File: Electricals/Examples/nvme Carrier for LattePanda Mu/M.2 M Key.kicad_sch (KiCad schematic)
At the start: 85 parts, among them J100 Bus_M.2_Socket_M, J110 Bus_M.2_Socket_M, J120 Bus_M.2_Socket_M, J130 Bus_M.2_Socket_M, J140 Bus_M.2_Socket_M, J150 Bus_M.2_Socket_M

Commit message: Some small changes
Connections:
- net +3V3aa: now also R132.2; no longer R112.2
- net +3V3b: now also R112.2; no longer R122.2
- net +3V3bb: now also R142.2; no longer R132.2
- net +3V3c: now also R122.2; no longer R142.2
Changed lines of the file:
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@@
 			)
 		)
-		(property "Value" "+3V3c"
+		(property "Value" "+3V3bb"
 			(at 335.28 279.4 0)
 			(effects
@@
 			)
 		)
-		(property "Value" "+3V3bb"
+		(property "Value" "+3V3aa"
 			(at 163.83 275.59 0)
 			(effects
@@
 			)
 		)
-		(property "Value" "+3V3b"
+		(property "Value" "+3V3c"
 			(at 527.05 107.95 0)
 			(effects
@@
 			)
 		)
-		(property "Value" "+3V3aa"
+		(property "Value" "+3V3b"
 			(at 336.55 106.68 0)
 			(effects

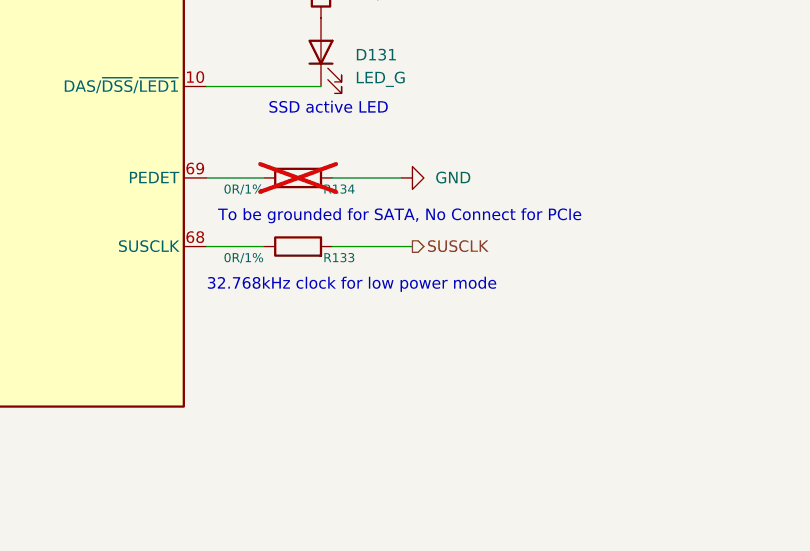
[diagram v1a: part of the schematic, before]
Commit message: Layout optimization + internal USB
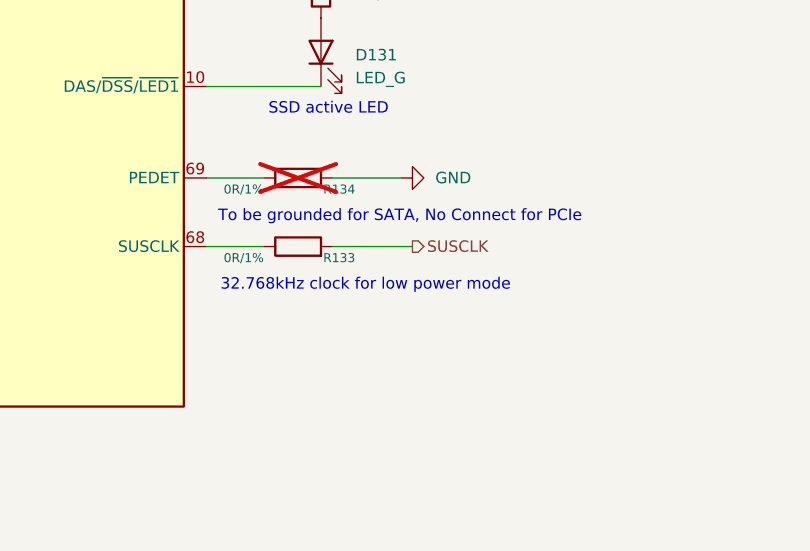
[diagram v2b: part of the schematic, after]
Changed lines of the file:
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@@
 	(text "32.768kHz clock for low power mode"
 		(exclude_from_sim no)
-		(at 151.13 318.77 0)
+		(at 152.654 318.77 0)
 		(effects
 			(font
